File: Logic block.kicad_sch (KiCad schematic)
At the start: 43 parts, among them J1 Conn_01x04_Socket, J14 Conn_01x04_Socket, J15 Conn_01x04_Socket, J16 Conn_01x02_Socket, J18 Conn_01x04_Socket, J2 Conn_01x04_Socket, J3 Conn_01x02_Socket, J4 Conn_01x04_Socket, J6 Conn_01x04_Socket, Q3 IRLZ44N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

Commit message: .
.
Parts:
- J1, J2, J4, J6: footprint (none) -> Connector_Phoenix_MC:PhoenixContact_MC_1,5_4-GF-3.81_1x04_P3.81mm_Horizontal_ThreadedFlange_MountHole
- J14: footprint (none) -> Connector_JST:JST_XH_B4B-XH-A_1x04_P2.50mm_Vertical
- J15, J18: footprint (none) -> Connector_JST:JST_XH_S4B-XH-A_1x04_P2.50mm_Horizontal
- J16: footprint (none) -> Connector_Phoenix_MC:PhoenixContact_MC_1,5_2-G-3.81_1x02_P3.81mm_Horizontal
- J3: footprint Connector:JWT_A3963_1x02_P3.96mm_Vertical -> Connector_JST:JST_XH_S2B-XH-A_1x02_P2.50mm_Horizontal
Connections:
- net at J1.4 (Pin_4), U3.1 (OB2): no longer J1.3 (Pin_3), U3.26 (OB1)
- new net: J1.3 (Pin_3), U3.26 (OB1)
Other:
- moved on the sheet: J1
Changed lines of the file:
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@@
 	)
 	(junction
-		(at 134.62 60.96)
-		(diameter 0)
-		(color 0 0 0 0)
-	)
-	(junction
 		(at 118.11 146.05)
 		(diameter 0)
@@
 	(wire
 		(pts
+			(xy 135.89 53.34) (xy 134.62 53.34)
+		)
+		(stroke
+			(width 0)
+			(type default)
+		)
+	)
+	(wire
+		(pts
 			(xy 139.7 146.05) (xy 143.51 146.05)
 		)
@@
 	(wire
 		(pts
+			(xy 135.89 58.42) (xy 134.62 58.42)
+		)
+		(stroke
+			(width 0)
+			(type default)
+		)
+	)
+	(wire
+		(pts
 			(xy 41.91 19.05) (xy 41.91 20.32)
 		)
@@
 	(wire
 		(pts
-			(xy 134.62 60.96) (xy 134.62 58.42)
+			(xy 135.89 55.88) (xy 134.62 55.88)
 		)
 		(stroke
@@
 	(wire
 		(pts
-			(xy 134.62 63.5) (xy 134.62 60.96)
-		)
-		(stroke
-			(width 0)
-			(type default)
-		)
-	)
-	(wire
-		(pts
 			(xy 102.87 118.11) (xy 102.87 120.65)
 		)
@@
 	(wire
 		(pts
+			(xy 135.89 60.96) (xy 135.89 63.5)
+		)
+		(stroke
+			(width 0)
+			(type default)
+		)
+	)
+	(wire
+		(pts
 			(xy 246.38 100.33) (xy 247.65 100.33)
 		)
@@
 	(wire
 		(pts
+			(xy 134.62 63.5) (xy 135.89 63.5)
+		)
+		(stroke
+			(width 0)
+			(type default)
+		)
+	)
+	(wire
+		(pts
 			(xy 116.84 24.13) (xy 116.84 25.4)
 		)
@@
 	(wire
 		(pts
+			(xy 134.62 58.42) (xy 134.62 60.96)
+		)
+		(stroke
+			(width 0)
+			(type default)
+		)
+	)
+	(wire
+		(pts
 			(xy 24.13 50.8) (xy 24.13 52.07)
 		)
@@
 		(polyline
 			(pts
-				(xy 265.43 165.1) (xy 284.48 165.1) (xy 284.48 135.89) (xy 265.43 135.89)
+				(xy 284.48 86.36) (xy 284.48 135.89) (xy 223.52 135.89) (xy 223.52 86.36)
 			)
 			(stroke
@@
 		(polyline
 			(pts
-				(xy 219.71 86.36) (xy 236.22 86.36) (xy 284.48 86.36) (xy 284.48 67.31) (xy 284.48 60.96) (xy 284.48 49.53)
-				(xy 284.48 49.53) (xy 284.48 38.1) (xy 284.48 30.48) (xy 284.48 21.59) (xy 284.48 16.51) (xy 284.48 12.7)
-				(xy 219.71 12.7)
+				(xy 180.34 62.23) (xy 219.71 62.23) (xy 219.71 12.7) (xy 180.34 12.7)
 			)
 			(stroke
@@
 		(polyline
 			(pts
-				(xy 284.48 86.36) (xy 284.48 135.89) (xy 223.52 135.89) (xy 223.52 86.36)
+				(xy 219.71 86.36) (xy 250.19 86.36) (xy 284.48 86.36) (xy 284.48 30.48) (xy 284.48 24.13) (xy 284.48 12.7)
+				(xy 284.48 12.7) (xy 267.97 12.7) (xy 257.81 12.7) (xy 255.27 12.7) (xy 255.27 12.7) (xy 254 12.7)
+				(xy 219.71 12.7)
 			)
 			(stroke
@@
 		(polyline
 			(pts
-				(xy 219.71 86.36) (xy 250.19 86.36) (xy 284.48 86.36) (xy 284.48 30.48) (xy 284.48 24.13) (xy 284.48 12.7)
-				(xy 284.48 12.7) (xy 267.97 12.7) (xy 257.81 12.7) (xy 255.27 12.7) (xy 255.27 12.7) (xy 254 12.7)
+				(xy 219.71 86.36) (xy 236.22 86.36) (xy 284.48 86.36) (xy 284.48 67.31) (xy 284.48 60.96) (xy 284.48 49.53)
+				(xy 284.48 49.53) (xy 284.48 38.1) (xy 284.48 30.48) (xy 284.48 21.59) (xy 284.48 16.51) (xy 284.48 12.7)
 				(xy 219.71 12.7)
 			)
@@
 		(polyline
 			(pts
-				(xy 180.34 62.23) (xy 219.71 62.23) (xy 219.71 12.7) (xy 180.34 12.7)
+				(xy 265.43 165.1) (xy 284.48 165.1) (xy 284.48 135.89) (xy 265.43 135.89)
 			)
 			(stroke
@@
 			)
 		)
-		(property "Footprint" ""
+		(property "Footprint" "Connector_Phoenix_MC:PhoenixContact_MC_1,5_4-GF-3.81_1x04_P3.81mm_Horizontal_ThreadedFlange_MountHole"
 			(at 139.7 123.19 0)
 			(effects
@@
 			)
 		)
-		(property "Footprint" ""
+		(property "Footprint" "Connector_JST:JST_XH_B4B-XH-A_1x04_P2.50mm_Vertical"
 			(at 280.67 142.24 0)
 			(effects
@@
 	(symbol
 		(lib_id "Connector:Conn_01x04_Socket")
-		(at 139.7 55.88 0)
+		(at 140.97 55.88 0)
 		(unit 1)
 		(exclude_from_sim no)
@@
 		(fields_autoplaced yes)
 		(property "Reference" "J1"
-			(at 140.97 55.8799 0)
+			(at 142.24 55.8799 0)
 			(effects
 				(font
@@
 		)
 		(property "Value" "Conn_01x04_Socket"
-			(at 140.97 58.4199 0)
+			(at 142.24 58.4199 0)
 			(effects
 				(font
@@
 			)
 		)
-		(property "Footprint" ""
-			(at 139.7 55.88 0)
+		(property "Footprint" "Connector_Phoenix_MC:PhoenixContact_MC_1,5_4-GF-3.81_1x04_P3.81mm_Horizontal_ThreadedFlange_MountHole"
+			(at 140.97 55.88 0)
 			(effects
 				(font
@@
 		)
 		(property "Datasheet" "~"
-			(at 139.7 55.88 0)
+			(at 140.97 55.88 0)
 			(effects
 				(font
@@
 		)
 		(property "Description" "Generic connector, single row, 01x04, script generated"
-			(at 139.7 55.88 0)
+			(at 140.97 55.88 0)
 			(effects
 				(font
@@
 			)
 		)
-		(property "Footprint" ""
+		(property "Footprint" "Connector_Phoenix_MC:PhoenixContact_MC_1,5_4-GF-3.81_1x04_P3.81mm_Horizontal_ThreadedFlange_MountHole"
 			(at 63.5 120.65 0)
 			(effects
@@
 			)
 		)
-		(property "Footprint" ""
+		(property "Footprint" "Connector_JST:JST_XH_S4B-XH-A_1x04_P2.50mm_Horizontal"
 			(at 205.74 30.48 0)
 			(effects
@@
 			)
 		)
-		(property "Footprint" "Connector:JWT_A3963_1x02_P3.96mm_Vertical"
+		(property "Footprint" "Connector_JST:JST_XH_S2B-XH-A_1x02_P2.50mm_Horizontal"
 			(at 278.13 107.95 0)
 			(effects
@@
 			)
 		)
-		(property "Footprint" ""
+		(property "Footprint" "Connector_JST:JST_XH_S4B-XH-A_1x04_P2.50mm_Horizontal"
 			(at 203.2 45.72 0)
 			(effects
@@
 			)
 		)
-		(property "Footprint" ""
+		(property "Footprint" "Connector_Phoenix_MC:PhoenixContact_MC_1,5_2-G-3.81_1x02_P3.81mm_Horizontal"
 			(at 273.05 40.64 0)
 			(effects
@@
 			)
 		)
-		(property "Footprint" ""
+		(property "Footprint" "Connector_Phoenix_MC:PhoenixContact_MC_1,5_4-GF-3.81_1x04_P3.81mm_Horizontal_ThreadedFlange_MountHole"
 			(at 63.5 53.34 0)
 			(effects

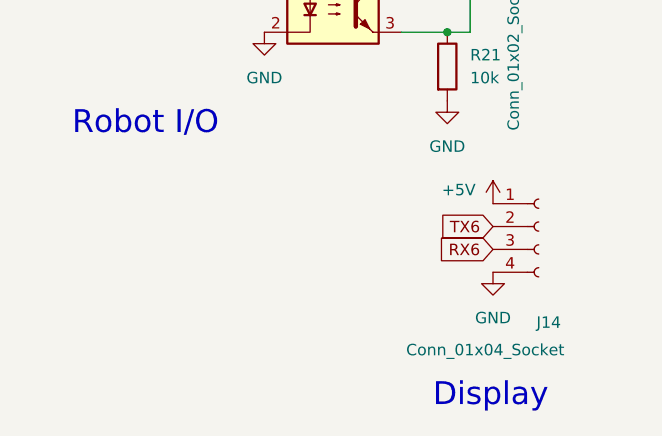
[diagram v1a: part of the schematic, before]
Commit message: RIP
reason of death
too much of board for too little time...
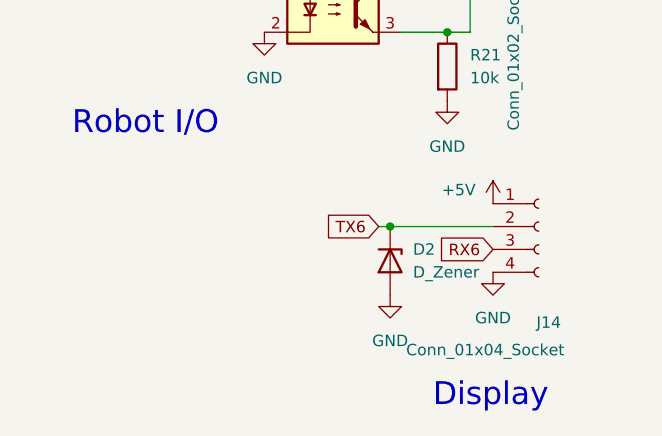
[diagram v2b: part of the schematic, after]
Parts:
- added D2: D_Zener, Diode_SMD:D_MiniMELF, symbol Device:D_Zener
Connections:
- net GND: now also D2.2 (A)
- net TX6: now also D2.1 (K)
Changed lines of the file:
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@@
 	)
 	(junction
+		(at 264.16 142.24)
+		(diameter 0)
+		(color 0 0 0 0)
+	)
+	(junction
 		(at 41.91 76.2)
 		(diameter 0)
@@
 	(wire
 		(pts
+			(xy 262.89 142.24) (xy 264.16 142.24)
+		)
+		(stroke
+			(width 0)
+			(type default)
+		)
+	)
+	(wire
+		(pts
 			(xy 24.13 118.11) (xy 24.13 119.38)
 		)
@@
 	(wire
 		(pts
+			(xy 264.16 142.24) (xy 275.59 142.24)
+		)
+		(stroke
+			(width 0)
+			(type default)
+		)
+	)
+	(wire
+		(pts
 			(xy 24.13 38.1) (xy 26.67 38.1)
 		)
@@
 	(global_label "TX6"
 		(shape input)
-		(at 275.59 142.24 180)
+		(at 262.89 142.24 180)
 		(fields_autoplaced yes)
 		(effects
@@
 		)
 		(property "Intersheetrefs" "${INTERSHEET_REFS}"
-			(at 269.2182 142.24 0)
+			(at 256.5182 142.24 0)
 			(effects
 				(font
@@
 		(polyline
 			(pts
-				(xy 284.48 86.36) (xy 284.48 135.89) (xy 223.52 135.89) (xy 223.52 86.36)
+				(xy 219.71 86.36) (xy 250.19 86.36) (xy 284.48 86.36) (xy 284.48 30.48) (xy 284.48 24.13) (xy 284.48 12.7)
+				(xy 284.48 12.7) (xy 267.97 12.7) (xy 257.81 12.7) (xy 255.27 12.7) (xy 255.27 12.7) (xy 254 12.7)
+				(xy 219.71 12.7)
 			)
 			(stroke
@@
 		(polyline
 			(pts
-				(xy 180.34 62.23) (xy 219.71 62.23) (xy 219.71 12.7) (xy 180.34 12.7)
+				(xy 284.48 86.36) (xy 284.48 135.89) (xy 223.52 135.89) (xy 223.52 86.36)
 			)
 			(stroke
@@
 		(polyline
 			(pts
-				(xy 219.71 86.36) (xy 250.19 86.36) (xy 284.48 86.36) (xy 284.48 30.48) (xy 284.48 24.13) (xy 284.48 12.7)
-				(xy 284.48 12.7) (xy 267.97 12.7) (xy 257.81 12.7) (xy 255.27 12.7) (xy 255.27 12.7) (xy 254 12.7)
-				(xy 219.71 12.7)
+				(xy 255.27 165.1) (xy 284.48 165.1) (xy 284.48 135.89) (xy 255.27 135.89)
 			)
 			(stroke
@@
 		(polyline
 			(pts
-				(xy 265.43 165.1) (xy 284.48 165.1) (xy 284.48 135.89) (xy 265.43 135.89)
+				(xy 180.34 62.23) (xy 219.71 62.23) (xy 219.71 12.7) (xy 180.34 12.7)
 			)
 			(stroke
@@
 	(symbol
 		(lib_id "power:GND")
+		(at 264.16 149.86 0)
+		(unit 1)
+		(exclude_from_sim no)
+		(in_bom yes)
+		(on_board yes)
+		(dnp no)
+		(fields_autoplaced yes)
+		(property "Reference" "#PWR0116"
+			(at 264.16 156.21 0)
+			(effects
+				(font
+					(size 1.27 1.27)
+				)
+				(hide yes)
+			)
+		)
+		(property "Value" "GND"
+			(at 264.16 154.94 0)
+			(effects
+				(font
+					(size 1.27 1.27)
+				)
+			)
+		)
+		(property "Footprint" ""
+			(at 264.16 149.86 0)
+			(effects
+				(font
+					(size 1.27 1.27)
+				)
+				(hide yes)
+			)
+		)
+		(property "Datasheet" ""
+			(at 264.16 149.86 0)
+			(effects
+				(font
+					(size 1.27 1.27)
+				)
+				(hide yes)
+			)
+		)
+		(property "Description" "Power symbol creates a global label with name \"GND\" , ground"
+			(at 264.16 149.86 0)
+			(effects
+				(font
+					(size 1.27 1.27)
+				)
+				(hide yes)
+			)
+		)
+		(pin "1"
+		)
+		(instances
+			(project "TechStarter"
+				(path "/7ea2363f-6757-4fc6-83f2-16ce190d79d1/9ccfbc8b-3421-4d2c-8f10-e495ba8db217"
+					(reference "#PWR0116")
+					(unit 1)
+				)
+			)
+		)
+	)
+	(symbol
+		(lib_id "power:GND")
 		(at 275.59 147.32 0)
 		(unit 1)
@@
 					(unit 1)
 				)
+			)
+		)
+	)
+	(symbol
+		(lib_id "Device:D_Zener")
+		(at 264.16 146.05 270)
+		(unit 1)
+		(exclude_from_sim no)
+		(in_bom yes)
+		(on_board yes)
+		(dnp no)
+		(fields_autoplaced yes)
+		(property "Reference" "D2"
+			(at 266.7 144.7799 90)
+			(effects
+				(font
+					(size 1.27 1.27)
+				)
+				(justify left)
+			)
+		)
+		(property "Value" "D_Zener"
+			(at 266.7 147.3199 90)
+			(effects
+				(font
+					(size 1.27 1.27)
+				)
+				(justify left)
+			)
+		)
+		(property "Footprint" "Diode_SMD:D_MiniMELF"
+			(at 264.16 146.05 0)
+			(effects
+				(font
+					(size 1.27 1.27)
+				)
+				(hide yes)
+			)
+		)
+		(property "Datasheet" "~"
+			(at 264.16 146.05 0)
+			(effects
+				(font
+					(size 1.27 1.27)
+				)
+				(hide yes)
+			)
+		)
+		(property "Description" "Zener diode"
+			(at 264.16 146.05 0)
+			(effects
+				(font
+					(size 1.27 1.27)
+				)
+				(hide yes)
+			)
+		)
+		(pin "2"
+		)
+		(pin "1"
+		)
+		(instances
+			(project ""
+				(path "/7ea2363f-6757-4fc6-83f2-16ce190d79d1/9ccfbc8b-3421-4d2c-8f10-e495ba8db217"
+					(reference "D2")
+					(unit 1)
+				)
